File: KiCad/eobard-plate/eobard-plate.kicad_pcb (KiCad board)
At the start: 2 copper layers, 119 x 109 mm, 19 parts

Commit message: Updated KiCad Files
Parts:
- moved G*** 0.28 mm to (147.0, 110.0)
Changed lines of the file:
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@@
   (title_block
     (title "Eobard Split Keyboard")
-    (date "2023-12-10")
-    (rev "2.2")
+    (date "2024-01-08")
+    (rev "1.1")
     (company "by viniciusbrit")
   )
@@
   )
   (footprint "Eobard-SVG-Files:ADHD-Creature" (layer "F.Cu")
-    (at 147.2 109.8)
+    (at 147 110)
     (attr board_only exclude_from_pos_files exclude_from_bom)
     (fp_text reference "G***" (at 0 -8.128) (layer "F.SilkS") hide

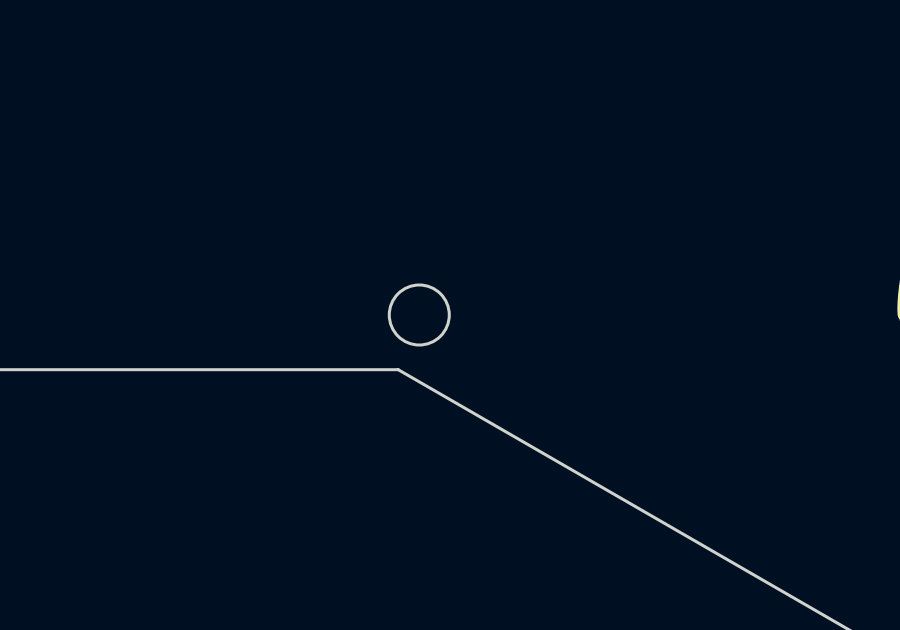
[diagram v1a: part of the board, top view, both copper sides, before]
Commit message: Fixed Silkscreen Error & Changed Mounting Hole Position
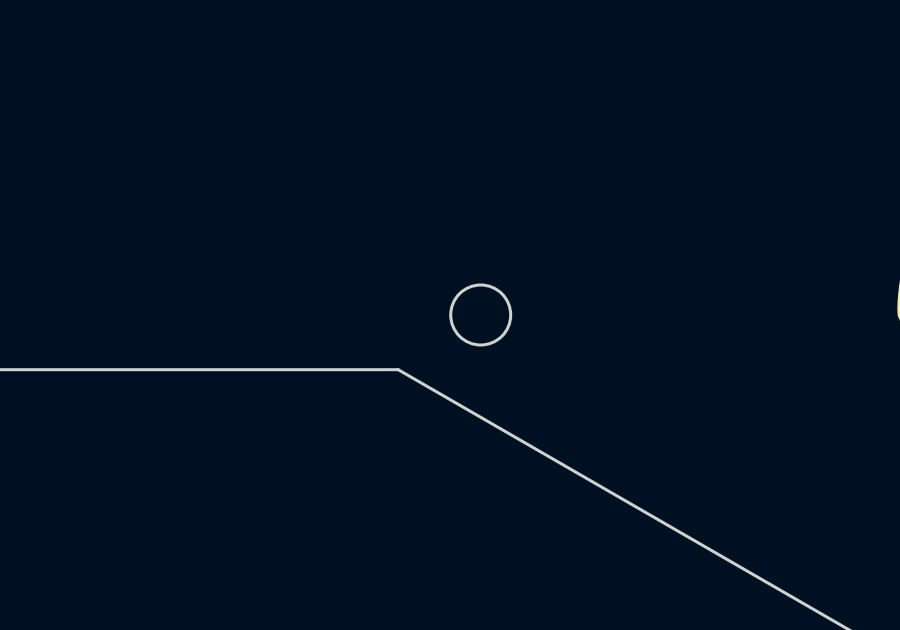
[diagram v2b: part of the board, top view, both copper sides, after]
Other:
- outline, holes or cut-outs redrawn
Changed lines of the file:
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@@
   (title_block
     (title "Eobard Split Keyboard")
-    (date "2024-01-08")
-    (rev "1.1")
+    (date "2024-01-12")
+    (rev "1.2")
     (company "by viniciusbrit")
   )
@@
   (gr_circle (center 176.5 106.5) (end 176.5 107.5)
     (stroke (width 0.1) (type default)) (fill none) (layer "Edge.Cuts"))
-  (gr_circle (center 123.952 109.6772) (end 124.952 109.6772)
+  (gr_circle (center 126 109.6772) (end 127 109.6772)
     (stroke (width 0.1) (type default)) (fill none) (layer "Edge.Cuts"))
   (gr_line (start 102 39) (end 78 52.5)
